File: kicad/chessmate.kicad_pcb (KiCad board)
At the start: 2 copper layers, 70 x 125.5 mm, 44 parts, among them J2 Power Jack, Q1 2N2222, Q2 2N2222, Q3 2N2222, Q4 2N2222, Q5 2N2222, SW1 F6, SW10 ENTER, SW11 CLEAR, SW12 H8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

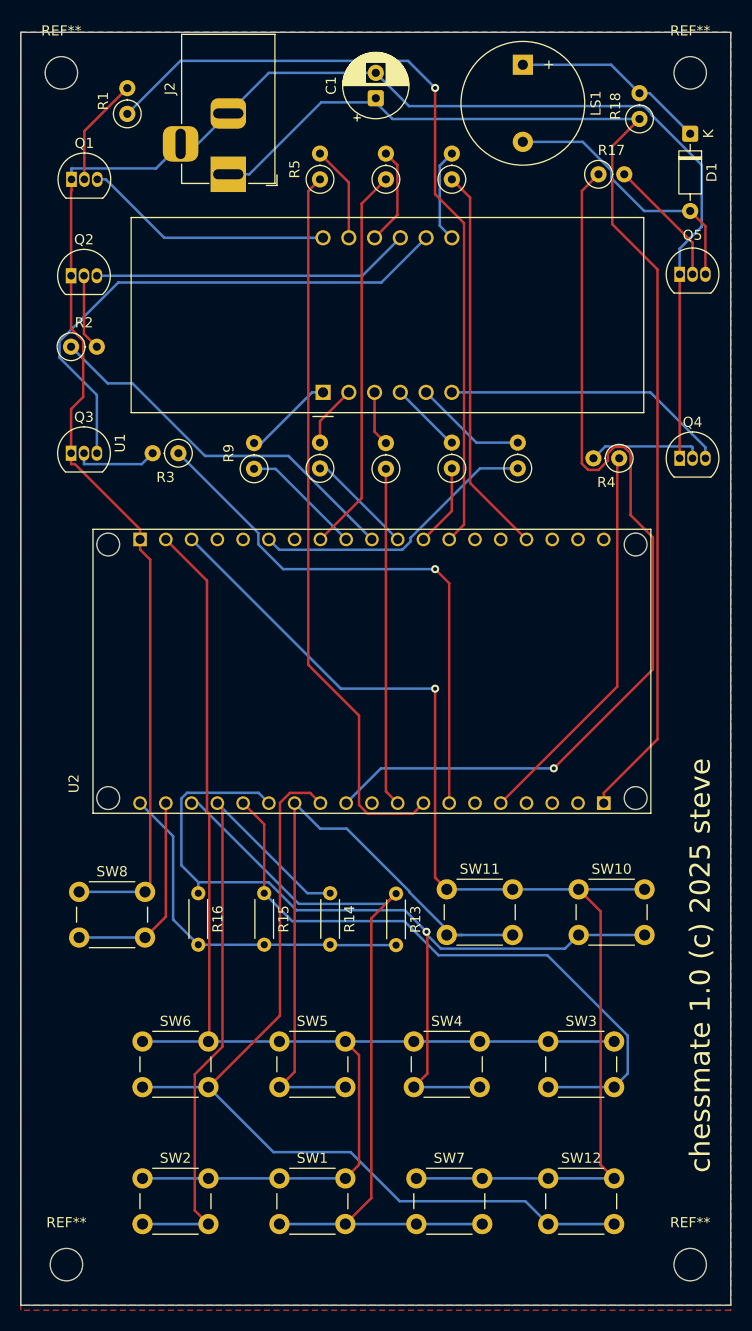
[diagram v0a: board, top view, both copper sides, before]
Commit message: replace 7-seg footprint with pin headers
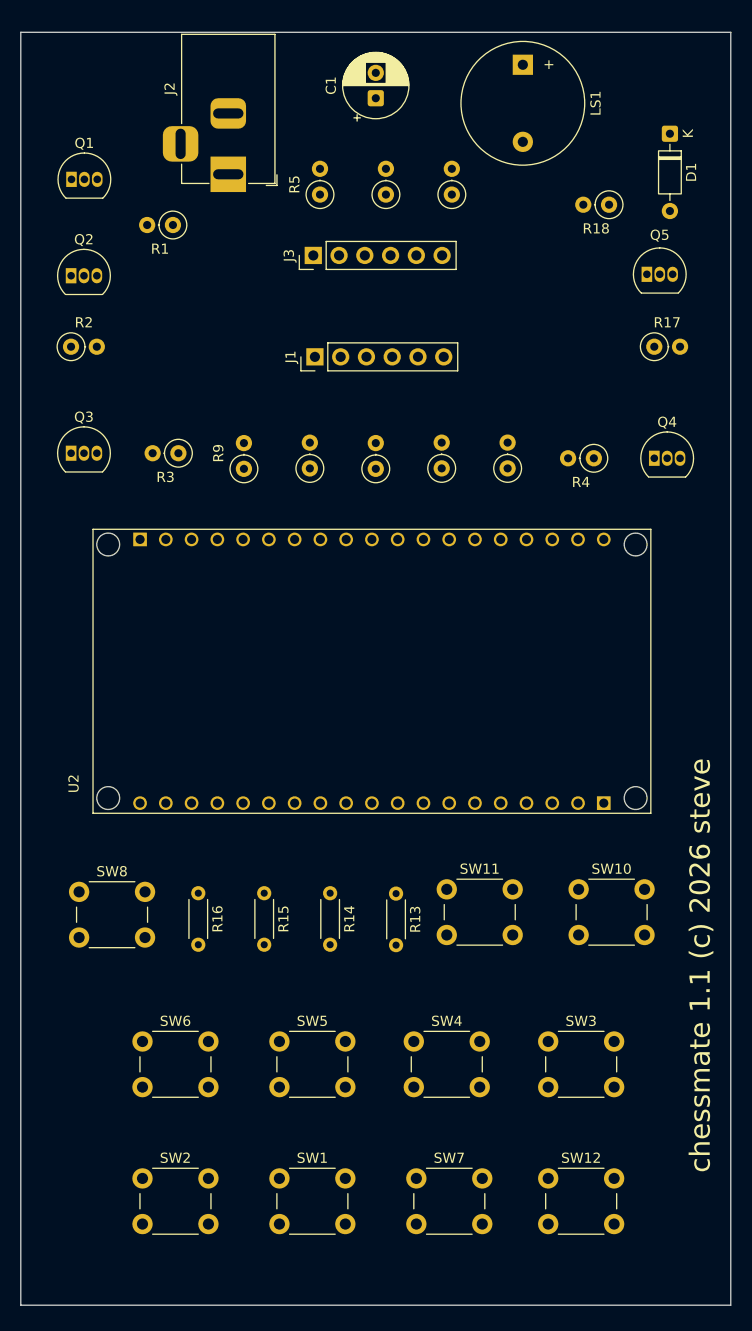
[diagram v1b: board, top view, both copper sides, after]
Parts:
- removed REF** (x4): MountingHole_3.2mm_M3, MountingHole:MountingHole_3.2mm_M3
- removed U1: CC56-12SURKWA, Display_7Segment:CA56-12SURKWA
- added J1: 7SegBtm, Connector_PinHeader_2.54mm:PinHeader_1x06_P2.54mm_Vertical, F.Cu at (79.0, 51.0)
- added J3: 7SegTop, Connector_PinHeader_2.54mm:PinHeader_1x06_P2.54mm_Vertical, F.Cu at (78.8, 41.0)
- moved R17 17.9 mm to (112.5, 50.0)
- moved R1 11.8 mm to (65.0, 38.0), turned to 180 degrees
- moved R18 8.97 mm to (108.0, 36.0), turned to 180 degrees
- moved Q5 3.23 mm to (111.7, 42.9)
- moved Q4 2.50 mm to (112.5, 61.0)
- moved R4 2.50 mm to (106.5, 61.0)
- moved D1 2.00 mm to (114.0, 29.0)
- moved R10 1.50 mm to (86.0, 35.0)
- moved R5 1.50 mm to (79.5, 35.0)
- moved R6 1.50 mm to (92.5, 35.0)
- moved R11 1.00 mm to (98.0, 62.0)
- moved R12 1.00 mm to (85.0, 62.0)
- moved R7 1.00 mm to (91.5, 62.0)
- moved R8 1.00 mm to (78.5, 62.0)
- moved R9 1.00 mm to (72.0, 62.0)
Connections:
- Q1 pad 3: /DIG1 -> D1
- Q2 pad 3: /DIG2 -> D2
- Q3 pad 3: /DIG3 -> D3
- Q4 pad 3: /DIG4 -> D4
- R10 pad 2: Net-(U1-f) -> F
- R11 pad 2: Net-(U1-g) -> G
- R12 pad 2: Net-(U1-DPX) -> DP
- R5 pad 2: Net-(U1-a) -> A
- R6 pad 2: Net-(U1-b) -> B
- R7 pad 2: Net-(U1-c) -> C
- R8 pad 2: Net-(U1-d) -> D
- R9 pad 2: Net-(U1-e) -> E
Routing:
- net GND: track 182.2 -> 0.00 mm
- net /ROW1_PIN: track 132.4 -> 0.00 mm
- net /ROW0_PIN: track 119.3 -> 0.00 mm, vias 1 -> 0
- net +5V: track 117.2 -> 0.00 mm
- net /SOUND_PIN: track 93.8 -> 0.00 mm, vias 1 -> 0
- net /COL3_PIN: track 89.1 -> 0.00 mm, vias 1 -> 0
- net /COL5_PIN: track 87.9 -> 0.00 mm
- net /DIG1_PIN: track 79.9 -> 0.00 mm, vias 1 -> 0
- net /COL0_PIN: track 79.5 -> 0.00 mm
- net /SEGA_PIN: track 71.4 -> 0.00 mm
- net /COL1_PIN: track 64.7 -> 0.00 mm
- net /COL2_PIN: track 63.5 -> 0.00 mm
- net /COL4_PIN: track 63.5 -> 0.00 mm
- net /DIG3_PIN: track 54.3 -> 0.00 mm, vias 1 -> 0
- net /DIG3: track 52.9 -> 0.00 mm
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- removed copper zone on F.Cu, net +3V3
- removed copper zone on B.Cu, net GND
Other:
- board text added: "3461AS-1"
- board text added: "chessmate 1.1 (c) 2026 steve"
- board text removed: "chessmate 1.0 (c) 2025 steve"

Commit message: update nodemcu footprint
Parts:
- removed U2: ESP32_NODEMCU, esp32-nodemcu:ESP32_NODEMCU
- added U1: AI-Thinker Nodemcu-32S, kicad-nodemcu32S-main:ai-thinker nodemcu-32s, F.Cu at (62.3, 91.9)
- LS1: footprint Buzzer_Beeper:Buzzer_12x9.5RM7.6 -> stevelib:Buzzer_12x9.5RM7.0

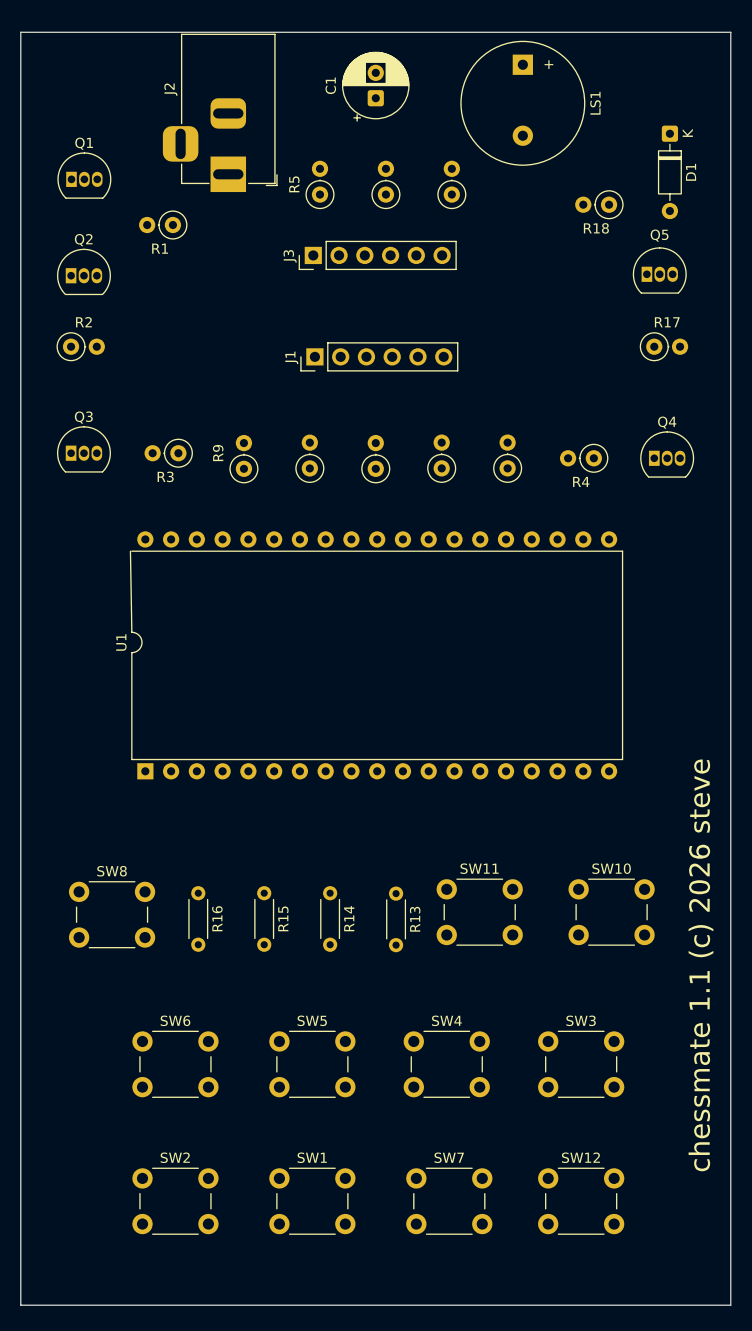
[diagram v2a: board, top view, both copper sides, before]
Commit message: move component values and switch names to F.Silkscreen layer
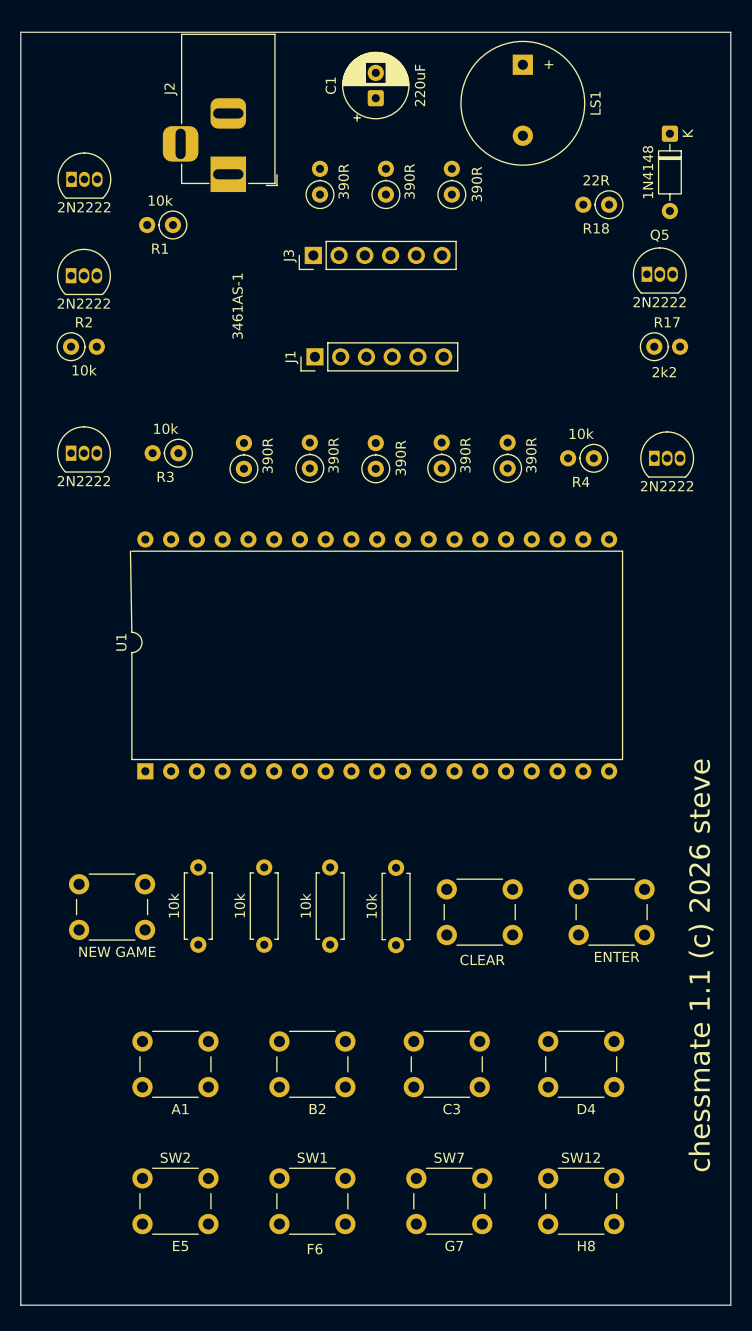
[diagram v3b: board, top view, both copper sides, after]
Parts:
- R13, R14, R15, R16: footprint Resistor_THT:R_Axial_DIN0204_L3.6mm_D1.6mm_P5.08mm_Horizontal -> Resistor_THT:R_Axial_DIN0207_L6.3mm_D2.5mm_P7.62mm_Horizontal
- moved R13 2.54 mm to (87.0, 101.4)
- moved R14 2.54 mm to (80.5, 101.3)
- moved R15 2.54 mm to (74.0, 101.3)
- moved R16 2.54 mm to (67.5, 101.3)
- moved SW8 0.75 mm to (55.8, 103.0)

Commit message: routing
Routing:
- net GND: track 0.00 -> 210.0 mm, vias 0 -> 1
- net /ROW1_PIN: track 0.00 -> 139.9 mm
- net /ROW0_PIN: track 0.00 -> 123.3 mm, vias 0 -> 1
- net +5V: track 0.00 -> 103.2 mm
- net /COL5_PIN: track 0.00 -> 97.1 mm, vias 0 -> 1
- net /COL3_PIN: track 0.00 -> 95.1 mm, vias 0 -> 1
- net /COL0_PIN: track 0.00 -> 80.9 mm
- net /SOUND_PIN: track 0.00 -> 69.8 mm, vias 0 -> 1
- net /SEGA_PIN: track 0.00 -> 67.0 mm, vias 0 -> 1
- net /COL2_PIN: track 0.00 -> 63.3 mm, vias 0 -> 1
- net /COL1_PIN: track 0.00 -> 63.1 mm, vias 0 -> 1
- net /DIG1_PIN: track 0.00 -> 62.5 mm, vias 0 -> 1
- net /COL4_PIN: track 0.00 -> 60.4 mm, vias 0 -> 1
- net /DIG3_PIN: track 0.00 -> 55.4 mm, vias 0 -> 1
- net /DIG2_PIN: track 0.00 -> 47.5 mm, vias 0 -> 1
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
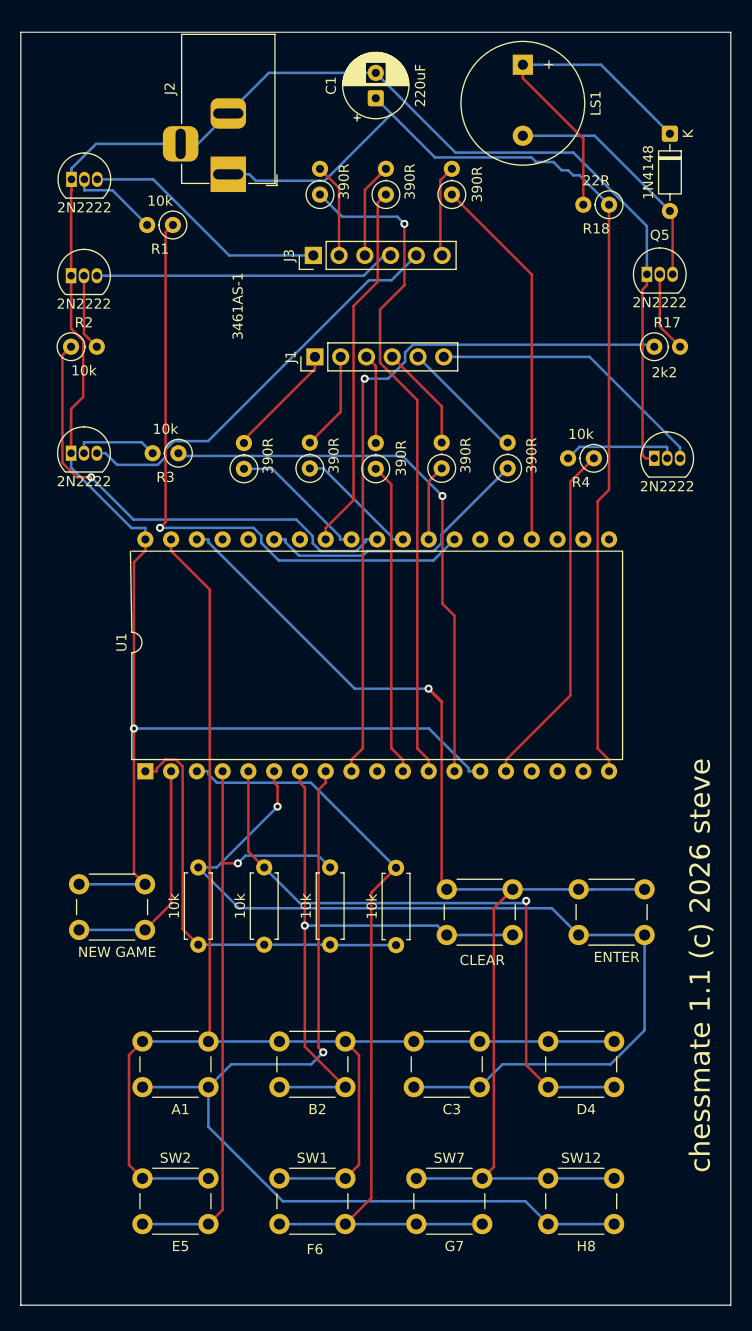
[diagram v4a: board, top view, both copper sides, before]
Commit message: add ground plane
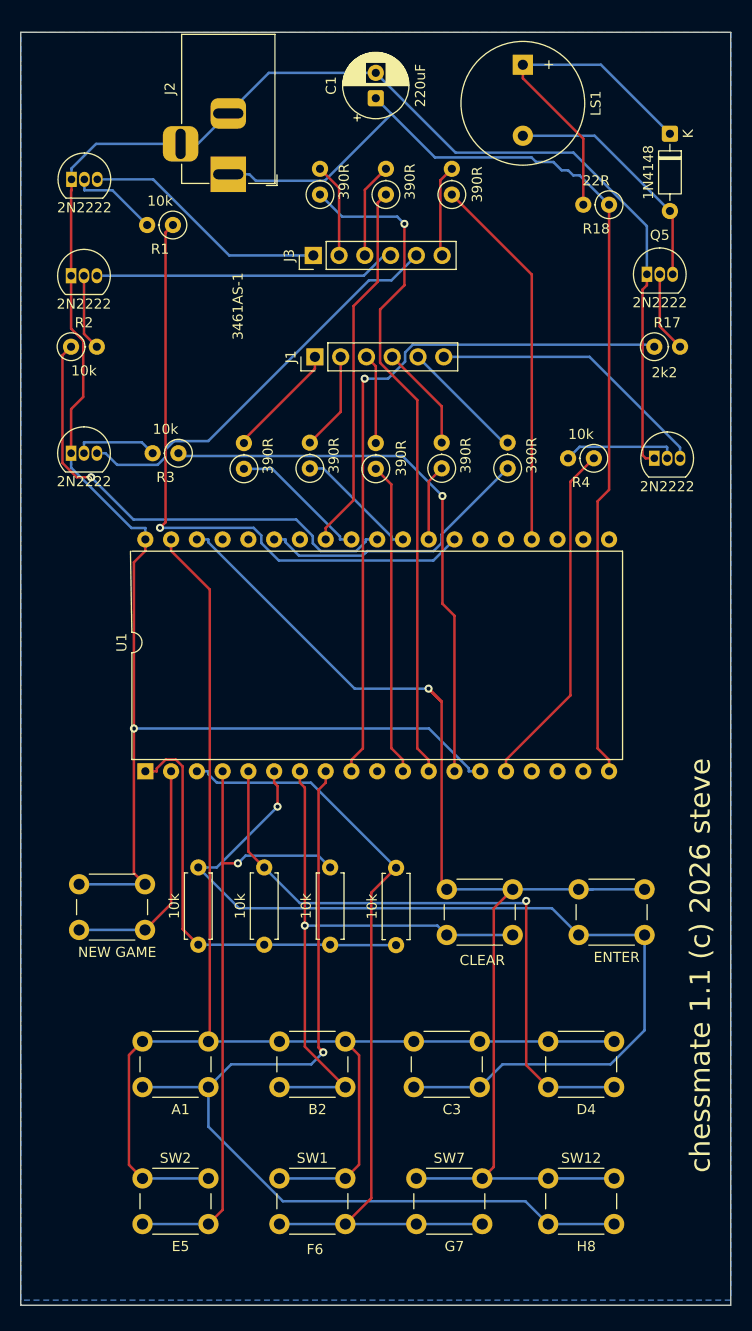
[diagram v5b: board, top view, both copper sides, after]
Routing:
- added copper zone on B.Cu, net GND
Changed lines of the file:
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@@
 		(net 44)
+	)
+	(zone
+		(net 2)
+		(net_name "GND")
+		(layer "B.Cu")
+		(hatch edge 0.5)
+		(connect_pads
+			(clearance 0.5)
+		)
+		(min_thickness 0.25)
+		(filled_areas_thickness no)
+		(fill yes
+			(thermal_gap 0.5)
+			(thermal_bridge_width 0.5)
+		)
+		(polygon
+			(pts
+				(xy 50 19) (xy 120 19) (xy 120 144) (xy 50 144)
+			)
+		)
 	)
 	(embedded_fonts no)

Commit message: add mounting holes
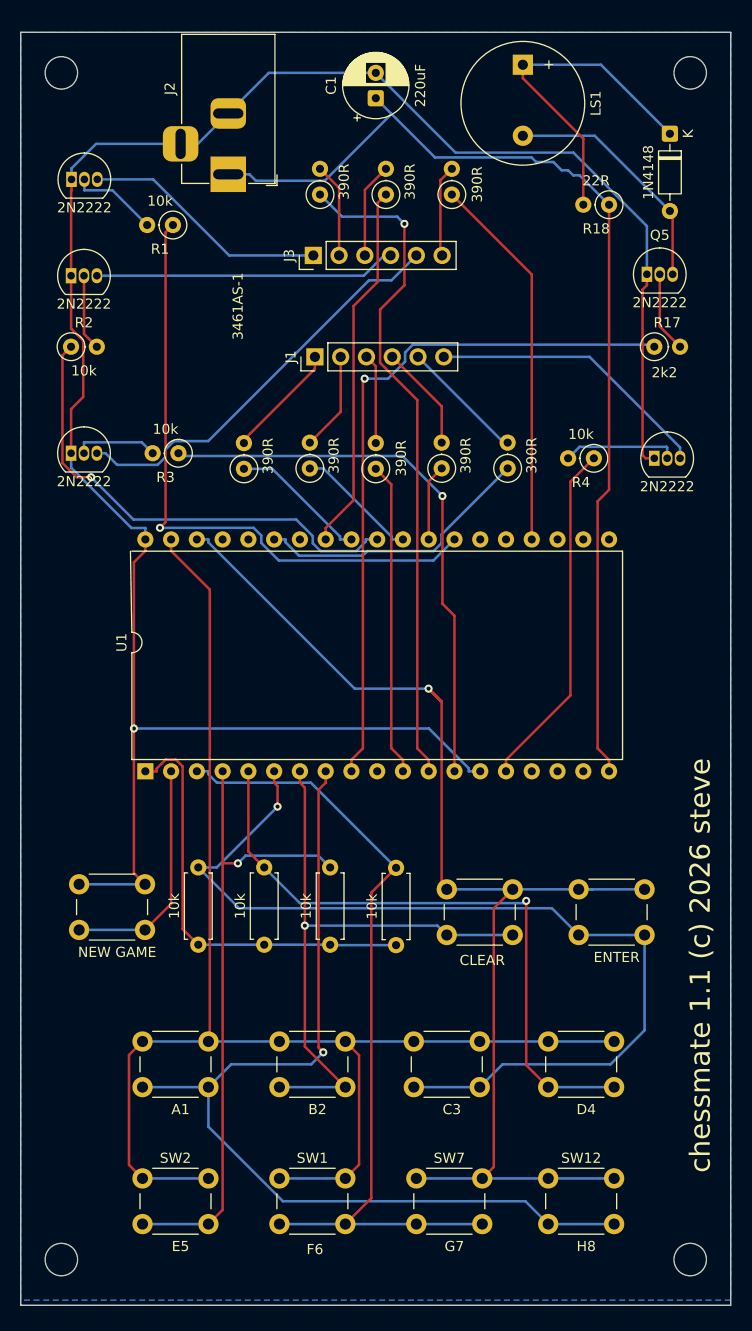
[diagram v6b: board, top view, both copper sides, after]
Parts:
- added REF**: MountingHole_3.2mm_M3, MountingHole:MountingHole_3.2mm_M3, F.Cu at (54.0, 23.0)
- added REF**: MountingHole_3.2mm_M3, MountingHole:MountingHole_3.2mm_M3, F.Cu at (116.0, 23.0)
- added REF**: MountingHole_3.2mm_M3, MountingHole:MountingHole_3.2mm_M3, F.Cu at (54.0, 140.0)
- added REF**: MountingHole_3.2mm_M3, MountingHole:MountingHole_3.2mm_M3, F.Cu at (116.0, 140.0)
